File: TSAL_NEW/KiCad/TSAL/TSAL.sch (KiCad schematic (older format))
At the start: 30 parts, among them J1 HV INPUT, J2 HV GND, J3 Green_LED_Jp, J4 Conn_02x02_Counter_Clockwise, Q1 BSS84, Q2 Q_PMOS_GSD, U1 LTV-817S, U2 LR8K4-G, U3 LM555, U4 LDB-350L

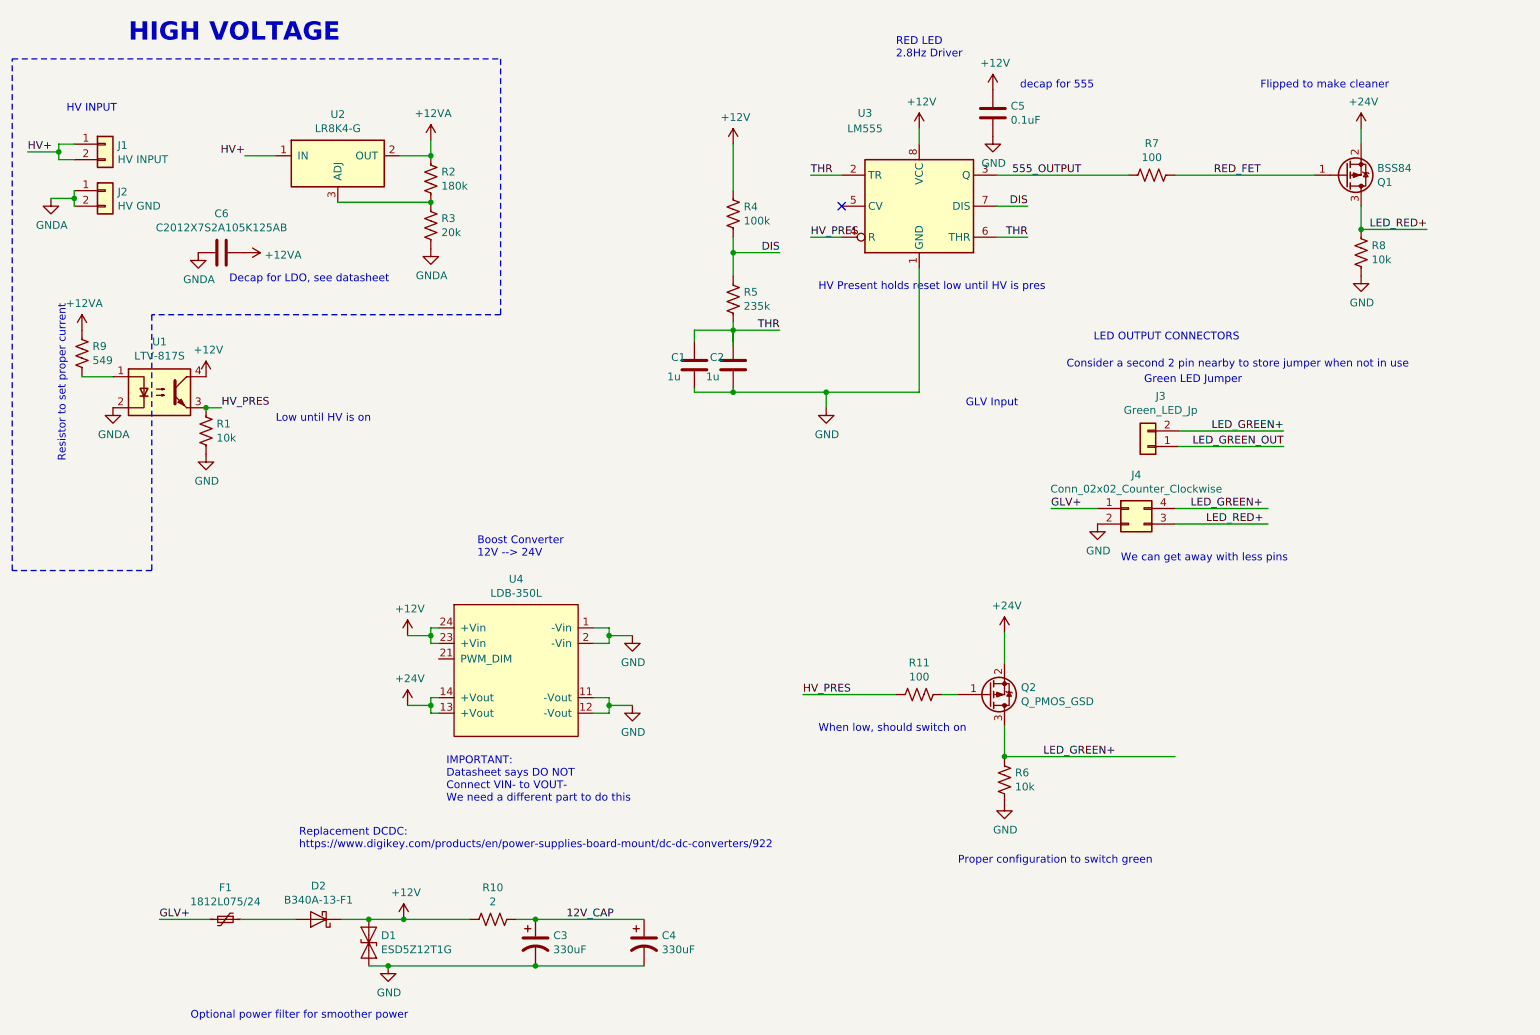
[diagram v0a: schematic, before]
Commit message: Final Schem - No Boost
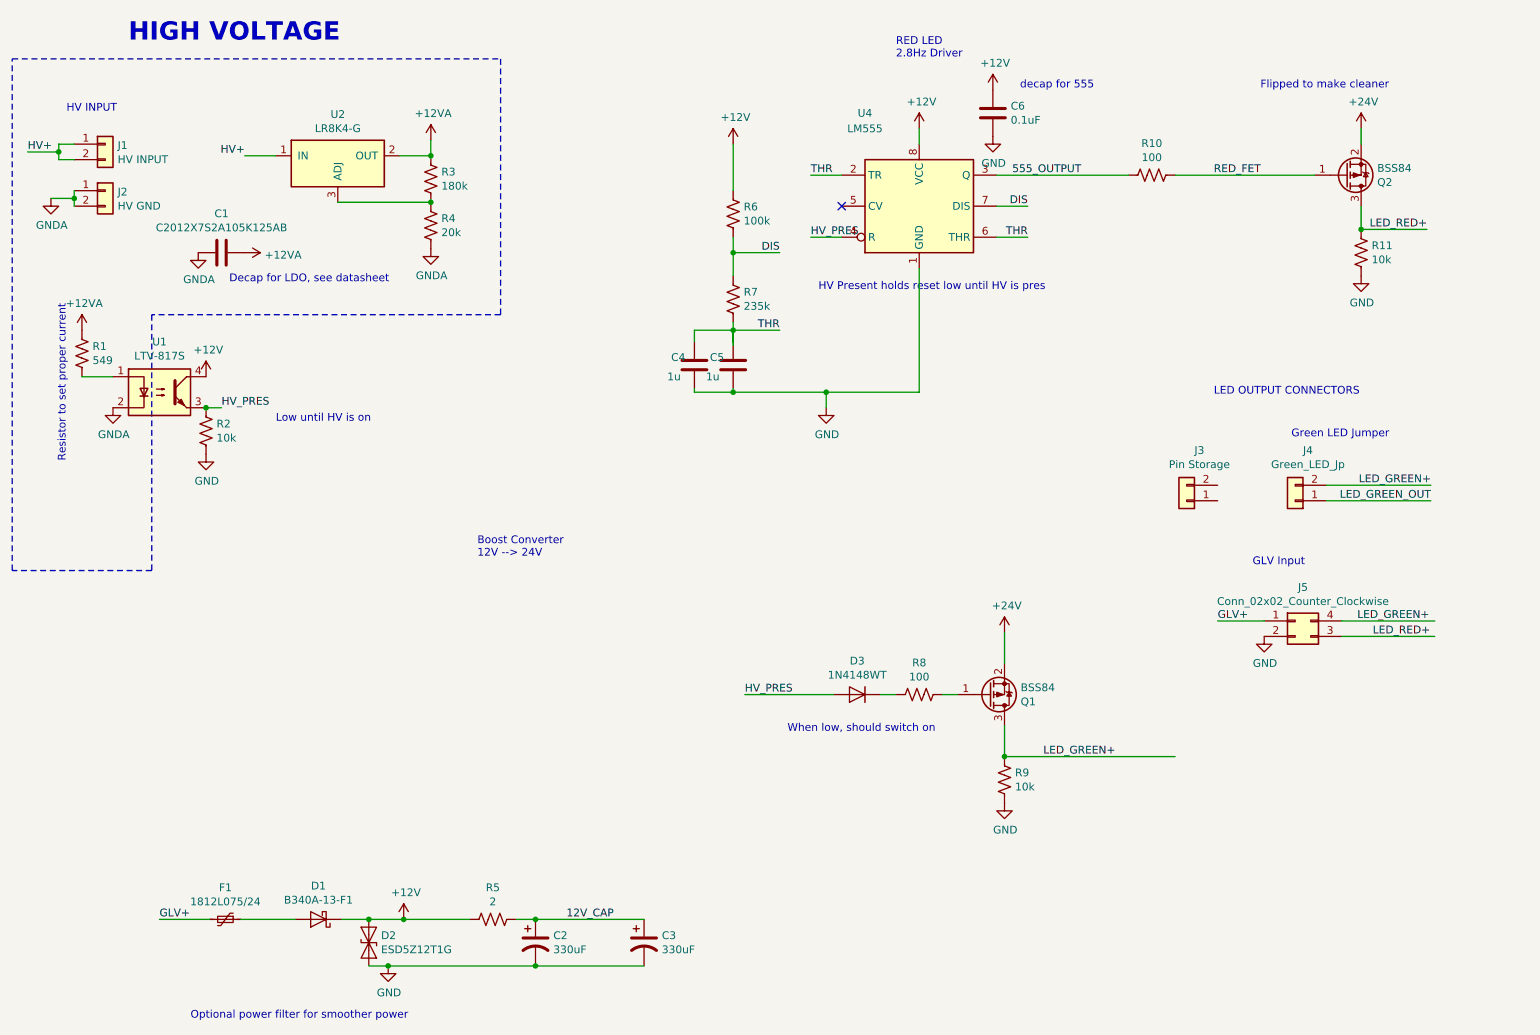
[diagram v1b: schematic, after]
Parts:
- removed Q2: Q_PMOS_GSD, symbol Device:Q_PMOS_GSD
- removed U4: LDB-350L, aero_footprint:LDB-_L, symbol TSAL-rescue:LDB-350L-AERO
- added D3: 1N4148WT, Diode_SMD:D_SOD-523, symbol Diode:1N4148WT
- added J3: Pin Storage, Connector_PinHeader_2.54mm:PinHeader_1x02_P2.54mm_Vertical, symbol Connector_Generic:Conn_01x02
- added Q1: BSS84, Package_TO_SOT_SMD:SOT-23, symbol Transistor_FET:BSS84
- J4: renamed from J3; footprint Connector_TE-Connectivity:TE_MATE-N-LOK_1-770866-x_1x02_P4.14mm_Vertical -> Connector_PinHeader_2.54mm:PinHeader_1x02_P2.54mm_Vertical
- R9: renamed from R6; footprint (none) -> Resistor_SMD:R_0603_1608Metric_Pad1.05x0.95mm_HandSolder
- renumbered C6 to C1, C3 to C2, C4 to C3, C1 to C4, C2 to C5, C5 to C6, D2 to D1, D1 to D2, J4 to J5, Q1 to Q2, R9 to R1, R7 to R10, R8 to R11, R1 to R2, R2 to R3, R3 to R4, R10 to R5, R4 to R6, R5 to R7, R11 to R8, U3 to U4
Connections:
- wire segments 81 -> 62
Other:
- note removed: "Consider a second 2 pin nearby to store jumper when not in use\n"
- note removed: "IMPORTANT:\nDatasheet says DO NOT\nConnect VIN- to VOUT-\nWe need a different part to do this"
- note removed: "Proper configuration to switch green"
- note removed: "Replacement DCDC:\nhttps://www.digikey.com/products/en/power-supplies-board-mount/dc-dc-converters/922"
- note removed: "We can get away with less pins"
- moved on the sheet: J4, J5

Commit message: Final PCB
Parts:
- added H1, H2: MountingHole, MountingHole:MountingHole_3mm, symbol Mechanical:MountingHole
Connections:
- net labels removed: +24V
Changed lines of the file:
@@
-	1    0    0    -1
-$EndComp
-$Comp
-L power:+24V #PWR019
-U 1 1 5E3B608A
-P 7300 4700
-F 0 "#PWR019" H 7300 4550 50  0001 C CNN
-F 1 "+24V" H 7315 4873 50  0000 C CNN
-F 2 "" H 7300 4700 50  0001 C CNN
-F 3 "" H 7300 4700 50  0001 C CNN
-	1    7300 4700
 	1    0    0    -1
 $EndComp
@@
 Wire Wire Line
 	7300 5500 7300 5300
-Wire Wire Line
-	7300 4700 7300 4900
 Wire Wire Line
 	8400 1750 9300 1750
@@
 	5550 3150 6150 3150
 $Comp
-L power:+24V #PWR022
-U 1 1 5E366083
-P 9600 1450
-F 0 "#PWR022" H 9600 1300 50  0001 C CNN
-F 1 "+24V" H 9615 1623 50  0000 C CNN
-F 2 "" H 9600 1450 50  0001 C CNN
-F 3 "" H 9600 1450 50  0001 C CNN
-	1    9600 1450
-	1    0    0    -1
-$EndComp
-$Comp
 L Device:R_US R11
 U 1 1 5E3668AC
@@
 $EndComp
 Text Label 7550 5500 0    50   ~ 0
-LED_GREEN+
+LED_GREEN_OUT
 $Comp
 L Device:R_US R9
@@
 	-1   0    0    1
 $EndComp
+$Comp
+L power:+12V #PWR0101
+U 1 1 5E38A720
+P 7300 4725
+F 0 "#PWR0101" H 7300 4575 50  0001 C CNN
+F 1 "+12V" H 7315 4898 50  0000 C CNN
+F 2 "" H 7300 4725 50  0001 C CNN
+F 3 "" H 7300 4725 50  0001 C CNN
+	1    7300 4725
+	1    0    0    -1
+$EndComp
+Wire Wire Line
+	7300 4725 7300 4900
+$Comp
+L power:+12V #PWR0102
+U 1 1 5E3944AE
+P 9600 1450
+F 0 "#PWR0102" H 9600 1300 50  0001 C CNN
+F 1 "+12V" H 9615 1623 50  0000 C CNN
+F 2 "" H 9600 1450 50  0001 C CNN
+F 3 "" H 9600 1450 50  0001 C CNN
+	1    9600 1450
+	1    0    0    -1
+$EndComp
+$Comp
+L Mechanical:MountingHole H1
+U 1 1 5E3DC11D
+P 9625 5300
+F 0 "H1" H 9725 5346 50  0000 L CNN
+F 1 "MountingHole" H 9725 5255 50  0000 L CNN
+F 2 "MountingHole:MountingHole_3mm" H 9625 5300 50  0001 C CNN
+F 3 "~" H 9625 5300 50  0001 C CNN
+	1    9625 5300
+	1    0    0    -1
+$EndComp
+$Comp
+L Mechanical:MountingHole H2
+U 1 1 5E3E028D
+P 9625 5575
+F 0 "H2" H 9725 5621 50  0000 L CNN
+F 1 "MountingHole" H 9725 5530 50  0000 L CNN
+F 2 "MountingHole:MountingHole_3mm" H 9625 5575 50  0001 C CNN
+F 3 "~" H 9625 5575 50  0001 C CNN
+	1    9625 5575
+	1    0    0    -1
+$EndComp
 $EndSCHEMATC

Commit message: TSAL Review complete
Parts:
- removed J3: Pin Storage, Connector_PinHeader_2.54mm:PinHeader_1x02_P2.54mm_Vertical, symbol Connector_Generic:Conn_01x02
- removed J4: Green_LED_Jp, Connector_PinHeader_2.54mm:PinHeader_1x02_P2.54mm_Vertical, symbol Connector_Generic:Conn_01x02
- removed J5: Conn_02x02_Counter_Clockwise, Connector_TE-Connectivity:TE_MATE-N-LOK_1-770874-x_2x02_P4.14mm_Vertical, symbol Connector_Generic:Conn_02x02_Counter_Clockwise
- added F2: Fuse, TSAL:PCC-1_2-R, symbol Device:Fuse
- added J3: Conn_01x03, Connector_PinHeader_2.54mm:PinHeader_1x03_P2.54mm_Vertical, symbol Connector_Generic:Conn_01x03
- added J4: Conn_01x04, Connector_JST:JST_XH_B4B-XH-AM_1x04_P2.50mm_Vertical, symbol Connector_Generic:Conn_01x04
- added PS1: PDQE15-Q24-S24-D, CONV_PDQE15-Q24-S24-D, symbol TSAL:PDQE15-Q24-S24-D
- J2: footprint Connector_TE-Connectivity:TE_MATE-N-LOK_1-770866-x_1x02_P4.14mm_Vertical -> TSAL:TE_MATE-N-LOK_1-770866-x_1x02_P4.14mm_Vertical
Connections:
- net labels added: ADJ, FUSE+, HV+F, LGR_D, LGR_G+, OPT+
- wire segments 62 -> 63
- no-connect marks 1 -> 2
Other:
- note added: "If used then add comp. components\n"
- note added: "Jumper P/N: M7583-05\n"
- note added: "Nylon Screws Only\nM3 Screws\n"
- note added: "UNUSED FOR NOW, TEST LED\n"
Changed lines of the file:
@@
 EESchema Schematic File Version 4
+LIBS:TSAL-cache
 EELAYER 30 0
 EELAYER END
@@
 	1    0    0    -1
 $EndComp
-Text Label 2400 1625 2    50   ~ 0
-HV+
 Wire Wire Line
 	2600 1625 2400 1625
@@
 F 0 "J2" H 1580 1842 50  0000 L CNN
 F 1 "HV GND" H 1580 1751 50  0000 L CNN
-F 2 "Connector_TE-Connectivity:TE_MATE-N-LOK_1-770866-x_1x02_P4.14mm_Vertical" H 1500 1850 50  0001 C CNN
+F 2 "TSAL:TE_MATE-N-LOK_1-770866-x_1x02_P4.14mm_Vertical" H 1500 1850 50  0001 C CNN
 F 3 "~" H 1500 1850 50  0001 C CNN
 	1    1500 1850
@@
 Text Label 7350 1750 0    50   ~ 0
 555_OUTPUT
-$Comp
-L Connector_Generic:Conn_01x02 J4
-U 1 1 5E49F346
-P 9175 3850
-F 0 "J4" H 9093 3525 50  0000 C CNN
-F 1 "Green_LED_Jp" H 9093 3616 50  0000 C CNN
-F 2 "Connector_PinHeader_2.54mm:PinHeader_1x02_P2.54mm_Vertical" H 9175 3850 50  0001 C CNN
-F 3 "~" H 9175 3850 50  0001 C CNN
-	1    9175 3850
-	-1   0    0    1
-$EndComp
 $Comp
 L Transistor_FET:BSS84 Q2
@@
 Wire Wire Line
 	3425 6550 3200 6550
-$Comp
-L Connector_Generic:Conn_02x02_Counter_Clockwise J5
-U 1 1 5E34BFFF
-P 9175 4625
-F 0 "J5" H 9225 4842 50  0000 C CNN
-F 1 "Conn_02x02_Counter_Clockwise" H 9225 4751 50  0000 C CNN
-F 2 "Connector_TE-Connectivity:TE_MATE-N-LOK_1-770874-x_2x02_P4.14mm_Vertical" H 9175 4625 50  0001 C CNN
-F 3 "~" H 9175 4625 50  0001 C CNN
-	1    9175 4625
-	1    0    0    -1
-$EndComp
-Text Label 8675 4625 0    50   ~ 0
+Text Label 8475 4625 0    50   ~ 0
 GLV+
-Wire Wire Line
-	8675 4625 8975 4625
-Text Label 9575 4625 0    50   ~ 0
+Text Label 8475 4725 0    50   ~ 0
+LED_RED+
+Text Label 8475 4825 0    50   ~ 0
 LED_GREEN+
-Text Label 9675 4725 0    50   ~ 0
-LED_RED+
-Wire Wire Line
-	10075 4625 9475 4625
-Wire Wire Line
-	10075 4725 9475 4725
 $Comp
 L Device:C C1
@@
 L power:GND #PWR021
 U 1 1 5E399D67
-P 8975 4725
-F 0 "#PWR021" H 8975 4475 50  0001 C CNN
-F 1 "GND" H 8980 4552 50  0000 C CNN
-F 2 "" H 8975 4725 50  0001 C CNN
-F 3 "" H 8975 4725 50  0001 C CNN
-	1    8975 4725
+P 8975 4925
+F 0 "#PWR021" H 8975 4675 50  0001 C CNN
+F 1 "GND" H 8980 4752 50  0000 C CNN
+F 2 "" H 8975 4925 50  0001 C CNN
+F 3 "" H 8975 4925 50  0001 C CNN
+	1    8975 4925
 	1    0    0    -1
 $EndComp
@@
 $EndComp
 $Comp
-L Connector_Generic:Conn_01x02 J3
-U 1 1 5E388FB3
-P 8475 3850
-F 0 "J3" H 8393 3525 50  0000 C CNN
-F 1 "Pin Storage" H 8393 3616 50  0000 C CNN
-F 2 "Connector_PinHeader_2.54mm:PinHeader_1x02_P2.54mm_Vertical" H 8475 3850 50  0001 C CNN
-F 3 "~" H 8475 3850 50  0001 C CNN
-	1    8475 3850
-	-1   0    0    1
-$EndComp
-$Comp
 L power:+12V #PWR0101
 U 1 1 5E38A720
@@
 	1    0    0    -1
 $EndComp
+$Comp
+L Connector_Generic:Conn_01x03 J3
+U 1 1 5E37818F
+P 9175 3850
+F 0 "J3" H 9093 4167 50  0000 C CNN
+F 1 "Conn_01x03" H 9093 4076 50  0000 C CNN
+F 2 "Connector_PinHeader_2.54mm:PinHeader_1x03_P2.54mm_Vertical" H 9175 3850 50  0001 C CNN
+F 3 "~" H 9175 3850 50  0001 C CNN
+	1    9175 3850
+	-1   0    0    -1
+$EndComp
+NoConn ~ 9375 3950
+Text Label 2425 6550 0    50   ~ 0
+FUSE+
+Text Label 3150 1925 0    50   ~ 0
+ADJ
+Text Label 1375 3050 0    50   ~ 0
+OPT+
+Text Label 6925 5100 0    50   ~ 0
+LGR_G+
+Text Label 6525 5100 0    50   ~ 0
+LGR_D
+$Comp
+L TSAL:PDQE15-Q24-S24-D PS1
+U 1 1 5E39A39A
+P 4100 4875
+F 0 "PS1" H 4100 5342 50  0000 C CNN
+F 1 "PDQE15-Q24-S24-D" H 4100 5251 50  0000 C CNN
+F 2 "CONV_PDQE15-Q24-S24-D" H 4100 4875 50  0001 L BNN
+F 3 "Manufacturer Recommendations" H 4100 4875 50  0001 L BNN
+F 4 "CUI Inc." H 4100 4875 50  0001 L BNN "Field4"
+F 5 "1.0" H 4100 4875 50  0001 L BNN "Field5"
+F 6 "11.70mm" H 4100 4875 50  0001 L BNN "Field6"
+	1    4100 4875
+	1    0    0    -1
+$EndComp
+Text Notes 3550 5450 0    50   ~ 0
+UNUSED FOR NOW, TEST LED\n
+Text Notes 9575 5875 0    50   ~ 0
+Nylon Screws Only\nM3 Screws\n
+Text Notes 3500 5550 0    50   ~ 0
+If used then add comp. components\n
+$Comp
+L Connector_Generic:Conn_01x04 J4
+U 1 1 5E37E507
+P 9175 4725
+F 0 "J4" H 9255 4717 50  0000 L CNN
+F 1 "Conn_01x04" H 9255 4626 50  0000 L CNN
+F 2 "Connector_JST:JST_XH_B4B-XH-AM_1x04_P2.50mm_Vertical" H 9175 4725 50  0001 C CNN
+F 3 "~" H 9175 4725 50  0001 C CNN
+	1    9175 4725
+	1    0    0    -1
+$EndComp
+Text Notes 7950 3875 0    50   ~ 0
+Jumper P/N: M7583-05\n
+Wire Wire Line
+	8475 4625 8975 4625
+Wire Wire Line
+	8975 4825 8475 4825
+Wire Wire Line
+	8475 4725 8975 4725
+$Comp
+L Device:Fuse F2
+U 1 1 5E3ADDA0
+P 2250 1625
+F 0 "F2" V 2053 1625 50  0000 C CNN
+F 1 "Fuse" V 2144 1625 50  0000 C CNN
+F 2 "TSAL:PCC-1_2-R" V 2180 1625 50  0001 C CNN
+F 3 "~" H 2250 1625 50  0001 C CNN
+	1    2250 1625
+	0    1    1    0
+$EndComp
+Text Label 1950 1625 0    50   ~ 0
+HV+
+Wire Wire Line
+	1950 1625 2100 1625
+Text Label 2400 1625 0    50   ~ 0
+HV+F
 $EndSCHEMATC
